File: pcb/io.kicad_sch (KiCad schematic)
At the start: 46 parts, among them J2 Conn_02x06_Counter_Clockwise, J3 Conn_02x06_Counter_Clockwise, U17 ESD224DQA, U18 ESD224DQA, U19 ESD224DQA, U20 ESD224DQA

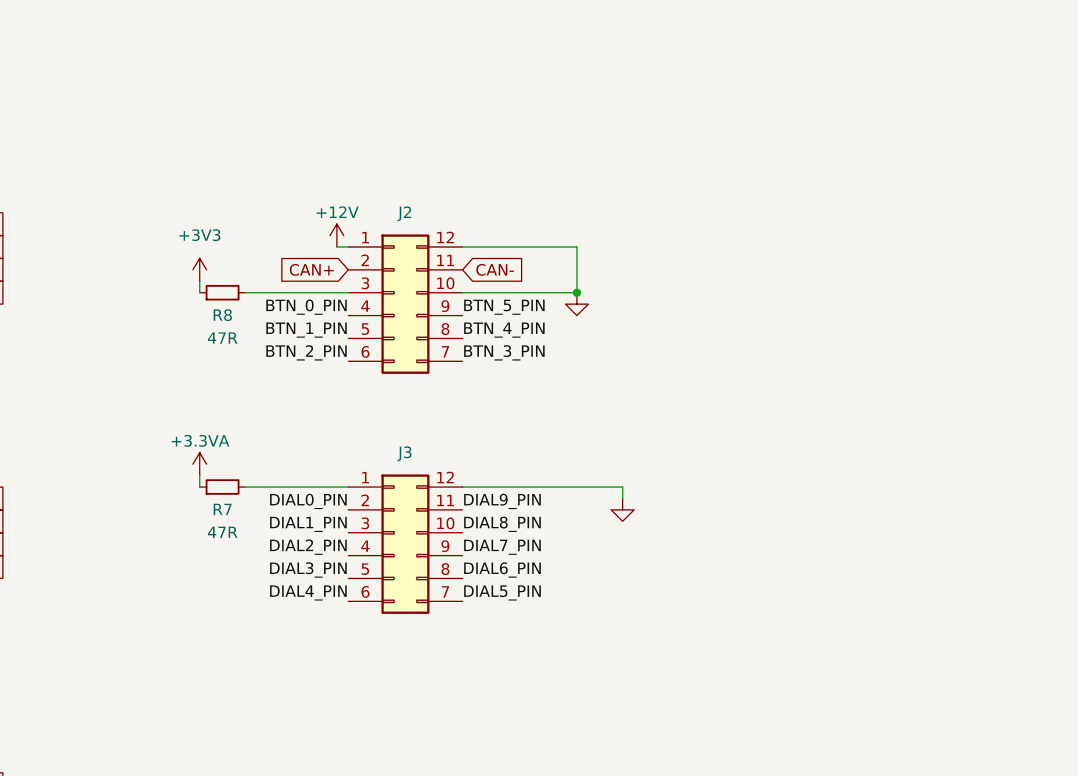
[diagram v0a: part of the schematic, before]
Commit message: Laid out and routed PCB
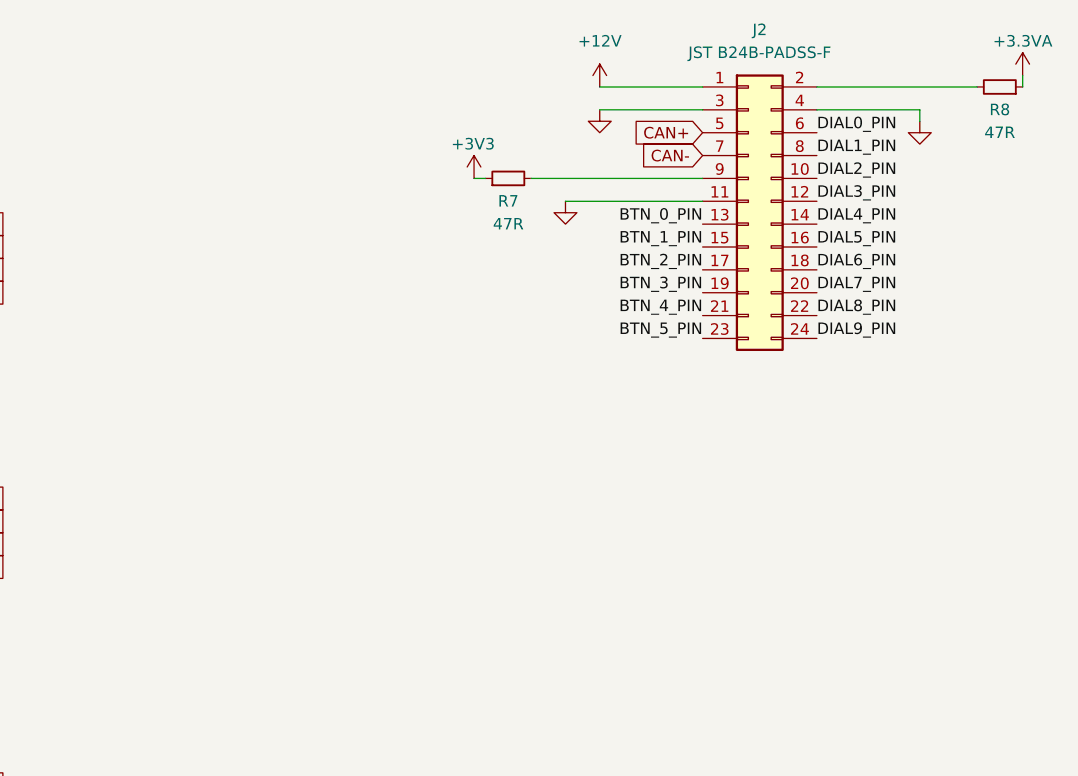
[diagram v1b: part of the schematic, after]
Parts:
- removed J2, J3: Conn_02x06_Counter_Clockwise, symbol Connector_Generic:Conn_02x06_Counter_Clockwise
- added J2: JST B24B-PADSS-F, Connector_JST:JST_PHD_B24B-PHDSS_2x12_P2.00mm_Vertical, symbol Connector_Generic:Conn_02x12_Odd_Even
- R7, R8: footprint (none) -> Resistor_SMD:R_0805_2012Metric
- RN13, RN14, RN15, RN16, RN17, RN18, RN19, RN20, RN21, RN22, RN23, RN24: footprint (none) -> Resistor_SMD:R_Array_Convex_4x0603
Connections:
- net +12V: now also J2.1 (Pin_1)
- net +3.3VA: now also R8.1; no longer R7.1
- net +3V3: now also R7.1; no longer R8.1
- net BTN_0_PIN: now also J2.13 (Pin_13)
- net BTN_1_PIN: now also J2.15 (Pin_15)
- net BTN_2_PIN: now also J2.17 (Pin_17)
- net BTN_3_PIN: now also J2.19 (Pin_19)
- net BTN_4_PIN: now also J2.21 (Pin_21)
- net BTN_5_PIN: now also J2.23 (Pin_23)
- net CAN+: now also J2.5 (Pin_5)
- net CAN-: now also J2.7 (Pin_7)
- net DIAL0_PIN: now also J2.6 (Pin_6)
- net DIAL1_PIN: now also J2.8 (Pin_8)
- net DIAL2_PIN: now also J2.10 (Pin_10)
- net DIAL3_PIN: now also J2.12 (Pin_12)
- net DIAL4_PIN: now also J2.14 (Pin_14)
- net DIAL5_PIN: now also J2.16 (Pin_16)
- net DIAL6_PIN: now also J2.18 (Pin_18)
- net DIAL7_PIN: now also J2.20 (Pin_20)
- net DIAL8_PIN: now also J2.22 (Pin_22)
- net DIAL9_PIN: now also J2.24 (Pin_24)
- net GND: now also J2.11 (Pin_11), J2.3 (Pin_3), J2.4 (Pin_4)
- net at R8.2: now also J2.2 (Pin_2)
- net at R7.2: now also J2.9 (Pin_9)

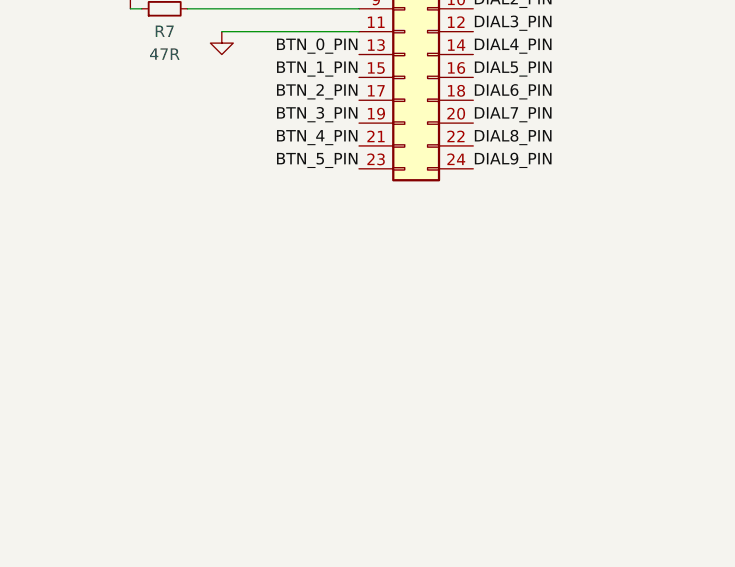
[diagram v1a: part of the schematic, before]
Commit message: Added debug/test header
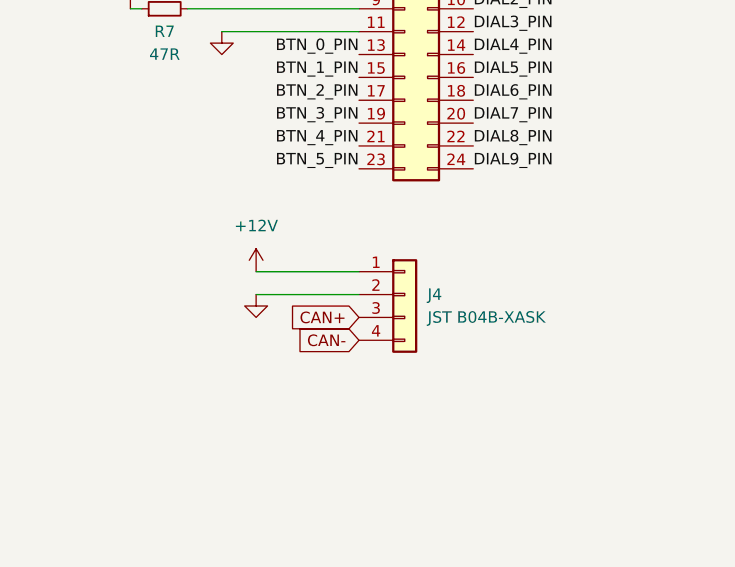
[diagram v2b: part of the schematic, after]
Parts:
- added J4: JST B04B-XASK, Connector_JST:JST_XA_B04B-XASK-1_1x04_P2.50mm_Vertical, symbol Connector_Generic:Conn_01x04
- J2: footprint Connector_JST:JST_PHD_B24B-PHDSS_2x12_P2.00mm_Vertical -> JST_B24B_PADSS:JST_B24B_PADSS
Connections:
- net +12V: now also J4.1 (Pin_1)
- net CAN+: now also J4.3 (Pin_3)
- net CAN-: now also J4.4 (Pin_4)
- net GND: now also J4.2 (Pin_2)
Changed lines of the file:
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@@
+    (stroke (width 0) (type default) (color 0 0 0 0))
+  )
+  (wire (pts (xy 217.17 91.44) (xy 228.6 91.44))
     (stroke (width 0) (type default) (color 0 0 0 0))
   )
@@
   )
   (wire (pts (xy 36.83 69.85) (xy 36.83 72.39))
+    (stroke (width 0) (type default) (color 0 0 0 0))
+  )
+  (wire (pts (xy 217.17 88.9) (xy 228.6 88.9))
     (stroke (width 0) (type default) (color 0 0 0 0))
   )
@@
     (property "Intersheet References" "${INTERSHEET_REFS}" (id 0) (at 150.7007 163.7506 0)
       (effects (font (size 1.27 1.27)) (justify left) hide)
+    )
+  )
+  (global_label "CAN-" (shape input) (at 228.6 96.52 180) (fields_autoplaced)
+    (effects (font (size 1.27 1.27)) (justify right))
+    (property "Intersheet References" "${INTERSHEET_REFS}" (id 0) (at 220.9255 96.5994 0)
+      (effects (font (size 1.27 1.27)) (justify right) hide)
     )
   )
@@
     )
   )
+  (global_label "CAN+" (shape input) (at 228.6 93.98 180) (fields_autoplaced)
+    (effects (font (size 1.27 1.27)) (justify right))
+    (property "Intersheet References" "${INTERSHEET_REFS}" (id 0) (at 220.9255 93.9006 0)
+      (effects (font (size 1.27 1.27)) (justify right) hide)
+    )
+  )
   (symbol (lib_id "Device:C_Small") (at 124.46 138.43 0) (unit 1)
     (in_bom yes) (on_board yes)
@@
     (property "Reference" "J2" (id 0) (at 234.95 43.18 0))
     (property "Value" "JST B24B-PADSS-F" (id 1) (at 234.95 45.72 0))
-    (property "Footprint" "Connector_JST:JST_PHD_B24B-PHDSS_2x12_P2.00mm_Vertical" (id 2) (at 233.68 62.23 0)
+    (property "Footprint" "JST_B24B_PADSS:JST_B24B_PADSS" (id 2) (at 234.95 81.28 0)
       (effects (font (size 1.27 1.27)) hide)
     )
@@
     (pin "1")
   )
+  (symbol (lib_id "Connector_Generic:Conn_01x04") (at 233.68 91.44 0) (unit 1)
+    (in_bom yes) (on_board yes) (fields_autoplaced)
+    (property "Reference" "J4" (id 0) (at 236.22 91.4399 0)
+      (effects (font (size 1.27 1.27)) (justify left))
+    )
+    (property "Value" "JST B04B-XASK" (id 1) (at 236.22 93.9799 0)
+      (effects (font (size 1.27 1.27)) (justify left))
+    )
+    (property "Footprint" "Connector_JST:JST_XA_B04B-XASK-1_1x04_P2.50mm_Vertical" (id 2) (at 233.68 91.44 0)
+      (effects (font (size 1.27 1.27)) hide)
+    )
+    (property "Datasheet" "~" (id 3) (at 233.68 91.44 0)
+      (effects (font (size 1.27 1.27)) hide)
+    )
+    (pin "1")
+    (pin "2")
+    (pin "3")
+    (pin "4")
+  )
   (symbol (lib_id "Jumper:Jumper_2_Bridged") (at 55.88 100.33 0) (unit 1)
     (in_bom yes) (on_board yes)
@@
     (pin "1")
   )
+  (symbol (lib_id "power:GND") (at 217.17 91.44 0) (mirror y) (unit 1)
+    (in_bom yes) (on_board yes) (fields_autoplaced)
+    (property "Reference" "#PWR?" (id 0) (at 217.17 97.79 0)
+      (effects (font (size 1.27 1.27)) hide)
+    )
+    (property "Value" "GND" (id 1) (at 217.17 96.52 0)
+      (effects (font (size 1.27 1.27)) hide)
+    )
+    (property "Footprint" "" (id 2) (at 217.17 91.44 0)
+      (effects (font (size 1.27 1.27)) hide)
+    )
+    (property "Datasheet" "" (id 3) (at 217.17 91.44 0)
+      (effects (font (size 1.27 1.27)) hide)
+    )
+    (pin "1")
+  )
   (symbol (lib_id "Jumper:Jumper_2_Bridged") (at 55.88 97.79 0) (unit 1)
     (in_bom yes) (on_board yes)
@@
     (pin "2")
   )
+  (symbol (lib_id "power:+12V") (at 217.17 88.9 0) (unit 1)
+    (in_bom yes) (on_board yes) (fields_autoplaced)
+    (property "Reference" "#PWR?" (id 0) (at 217.17 92.71 0)
+      (effects (font (size 1.27 1.27)) hide)
+    )
+    (property "Value" "+12V" (id 1) (at 217.17 83.82 0))
+    (property "Footprint" "" (id 2) (at 217.17 88.9 0)
+      (effects (font (size 1.27 1.27)) hide)
+    )
+    (property "Datasheet" "" (id 3) (at 217.17 88.9 0)
+      (effects (font (size 1.27 1.27)) hide)
+    )
+    (pin "1")
+  )
 )
